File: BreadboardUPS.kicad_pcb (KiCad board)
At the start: 2 copper layers, 39.2 x 81 mm, 78 parts, among them J101 Output, J104 Ctrl, J202 USBC, J203 DC In, J301 BAT, Q401 DO2308S, Q402 DO2309A, Q403 DO2309A, SW401 Vsel, SW402 PWR_ON, U201 TPS630701RNMR, U301 BQ24090DGQ, U302 BQ27441-G1, U401 TPS630701RNMR

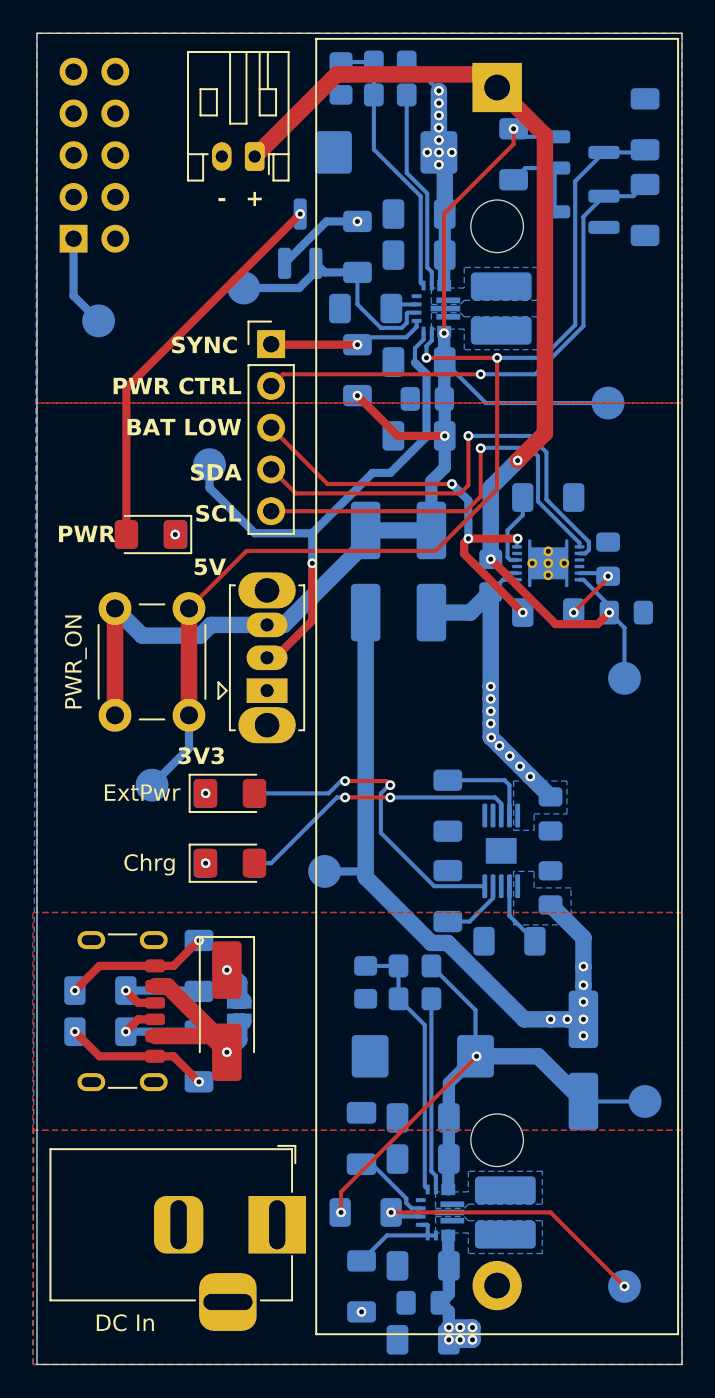
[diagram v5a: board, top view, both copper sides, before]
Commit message: Rounded PCB corners
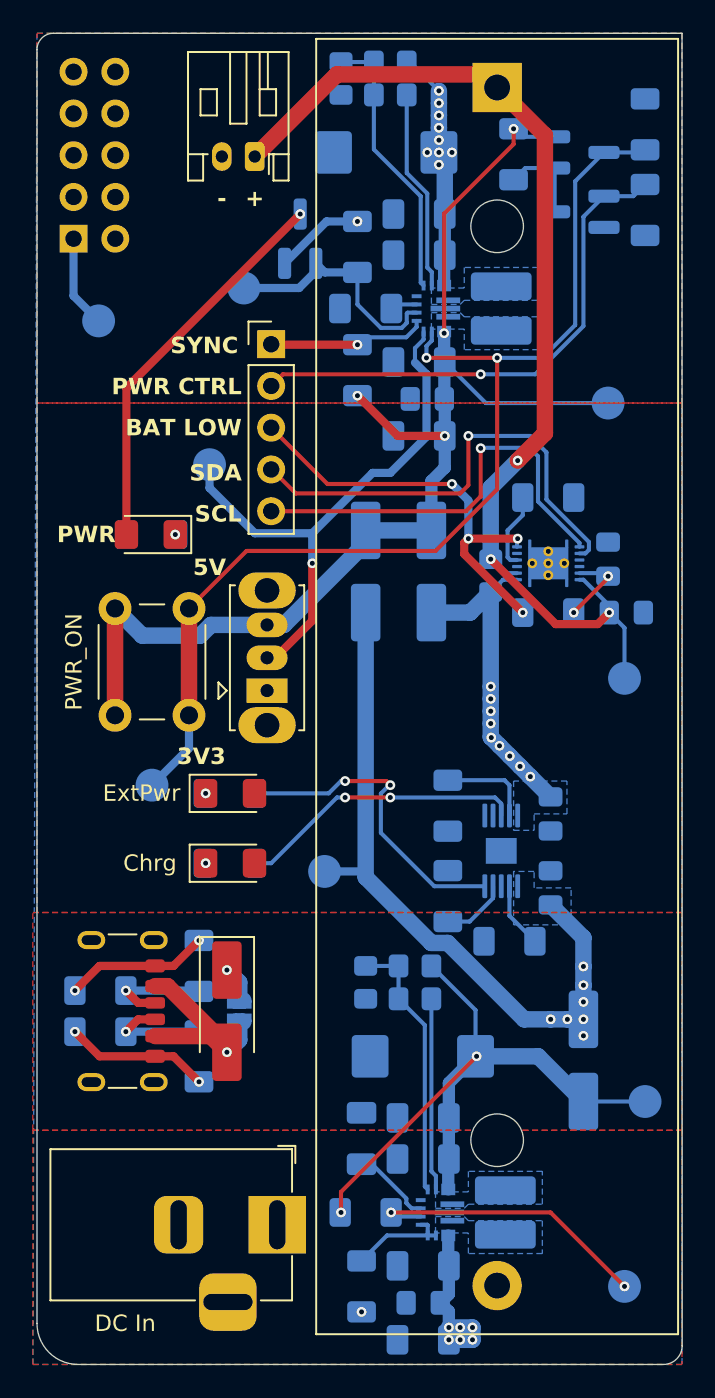
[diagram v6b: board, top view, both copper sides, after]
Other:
- board size 39.2 x 81 mm -> 39.3 x 81 mm
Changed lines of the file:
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@@
 		(embedded_fonts no)
 	)
-	(gr_rect
-		(start 120 72.25)
-		(end 159.25 153.25)
+	(gr_line
+		(start 121 72.25)
+		(end 159.25 72.25)
 		(stroke
 			(width 0.05)
 			(type default)
 		)
-		(fill no)
 		(layer "Edge.Cuts")
 	)
+	(gr_line
+		(start 120 150.75)
+		(end 120 73.25)
+		(stroke
+			(width 0.05)
+			(type default)
+		)
+		(layer "Edge.Cuts")
+	)
+	(gr_arc
+		(start 122.5 153.25)
+		(mid 120.732233 152.517767)
+		(end 120 150.75)
+		(stroke
+			(width 0.05)
+			(type solid)
+		)
+		(layer "Edge.Cuts")
+	)
+	(gr_line
+		(start 158.115 153.25)
+		(end 122.5 153.25)
+		(stroke
+			(width 0.05)
+			(type default)
+		)
+		(layer "Edge.Cuts")
+	)
+	(gr_arc
+		(start 120 73.25)
+		(mid 120.292893 72.542893)
+		(end 121 72.25)
+		(stroke
+			(width 0.05)
+			(type solid)
+		)
+		(layer "Edge.Cuts")
+	)
+	(gr_arc
+		(start 159.258 152.107)
+		(mid 158.923223 152.915223)
+		(end 158.115 153.25)
+		(stroke
+			(width 0.05)
+			(type default)
+		)
+		(layer "Edge.Cuts")
+	)
+	(gr_line
+		(start 159.25 72.25)
+		(end 159.258 152.107)
+		(stroke
+			(width 0.05)
+			(type default)
+		)
+		(layer "Edge.Cuts")
+	)

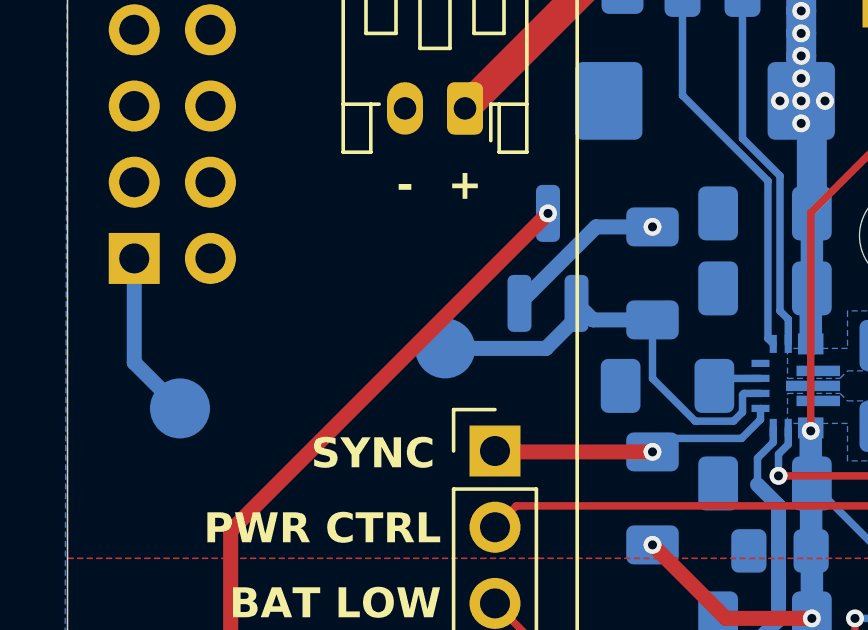
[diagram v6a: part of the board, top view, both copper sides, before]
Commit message: Add version to silkscreen
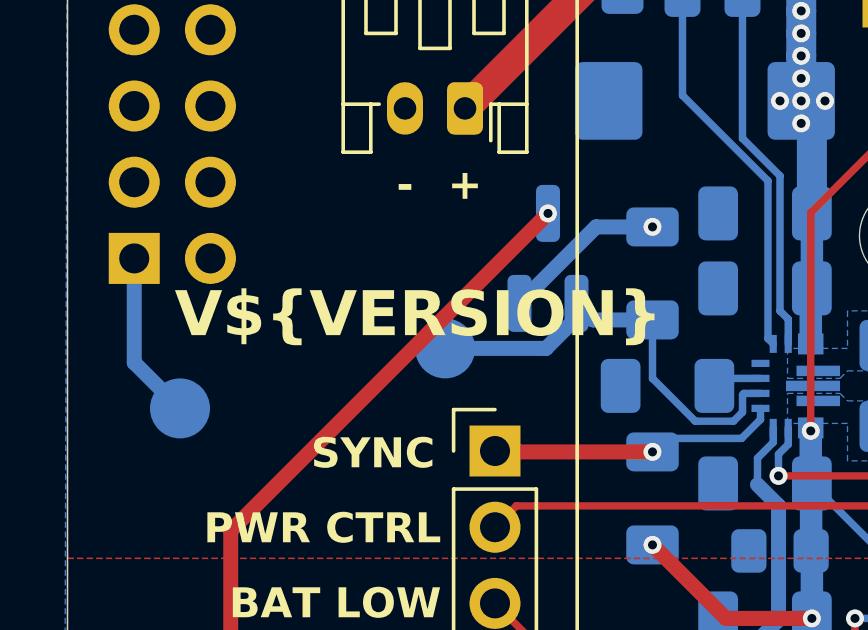
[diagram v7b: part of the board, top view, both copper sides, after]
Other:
- board text added: "V${VERSION}"
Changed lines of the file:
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@@
 		)
 	)
+	(property "VERSION" "01.00")
 	(net 0 "")
 	(net 1 "GND")
@@
 		)
 	)
+	(gr_text "V${VERSION}"
+		(at 131.699 86.614 0)
+		(layer "F.SilkS")
+		(effects
+			(font
+				(size 1.5 1.5)
+				(thickness 0.3)
+				(bold yes)
+			)
+		)
+	)
